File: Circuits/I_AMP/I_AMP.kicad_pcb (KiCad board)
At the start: 2 copper layers, 98 x 61 mm, 44 parts, among them P1 INPUT, P2 POWER, P5 GAIN ON/OFF, P6 OUTPUT (0-5V), U1 TL062, U2 LM393, U3 OPA277

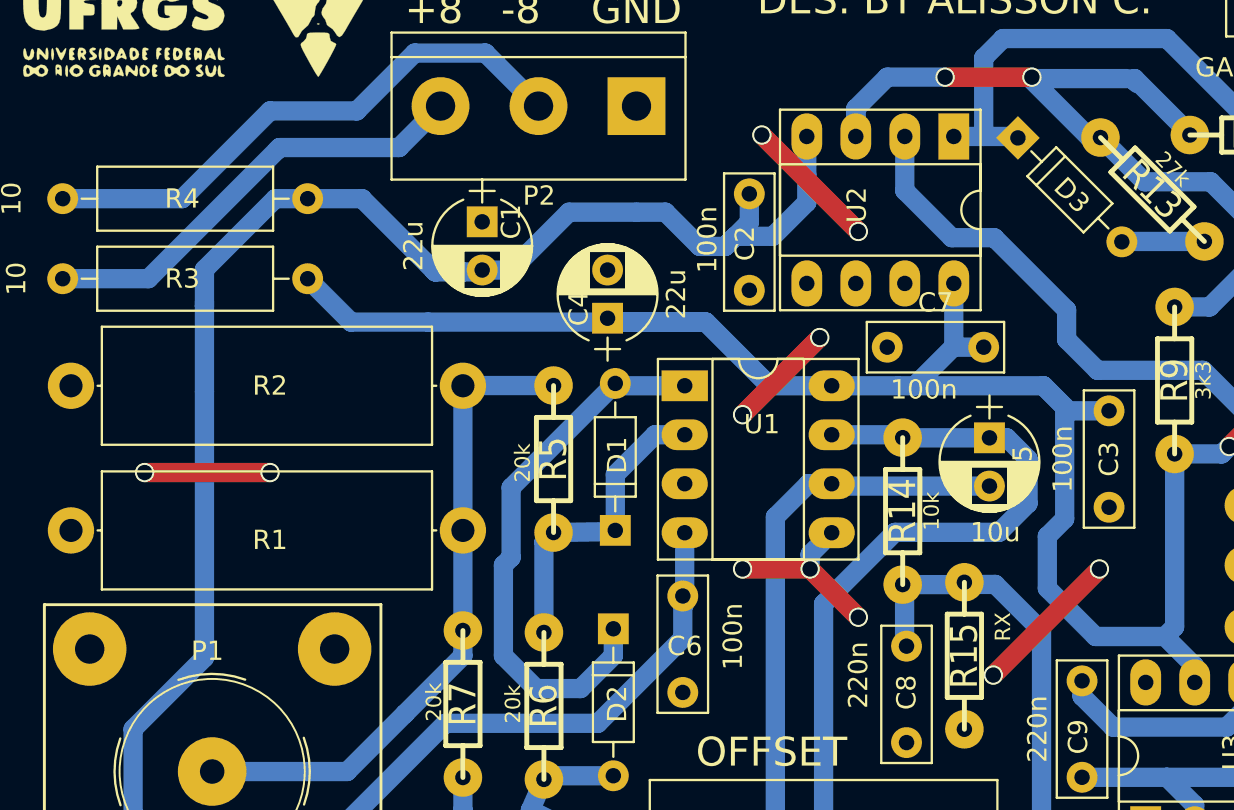
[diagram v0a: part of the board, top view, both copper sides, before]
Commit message: EDIT: Correction of some jumpers
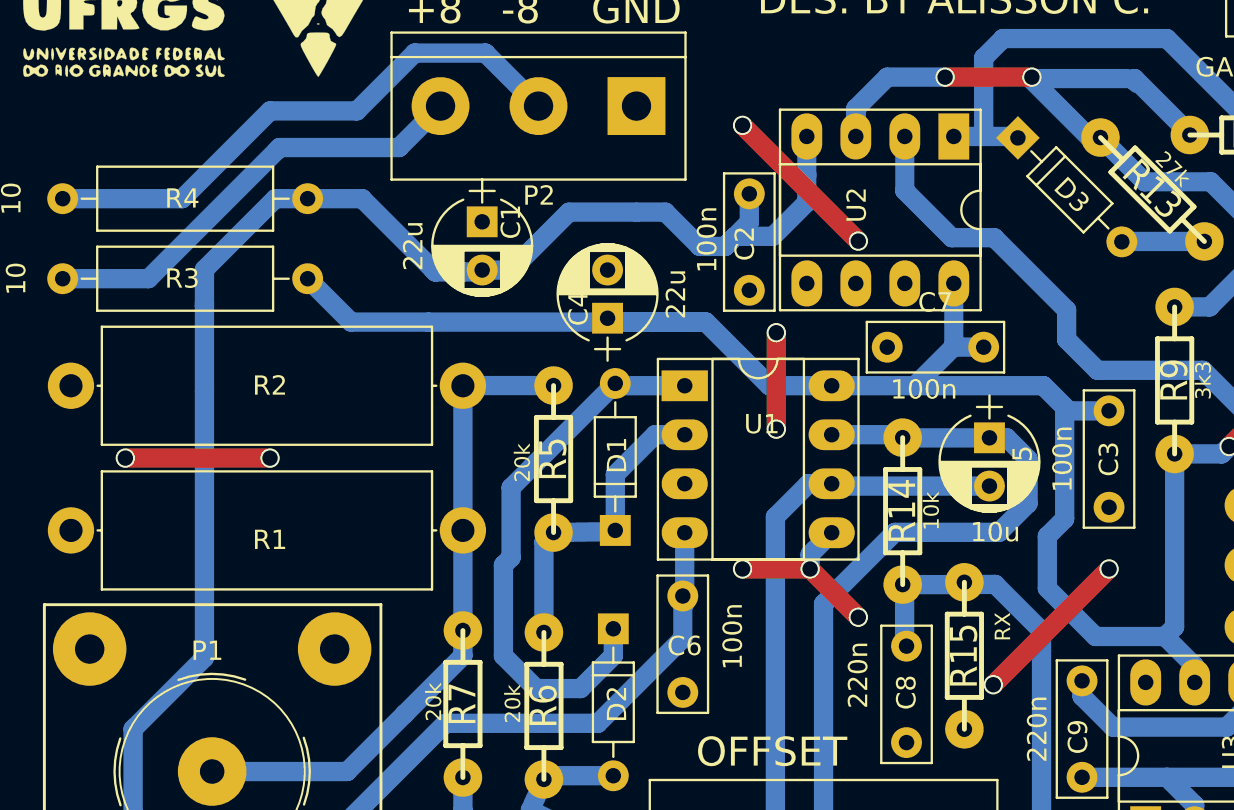
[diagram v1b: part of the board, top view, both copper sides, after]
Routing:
- net GND: track 36.4 -> 38.9 mm
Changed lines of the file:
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@@
   )
   (gr_line (start 67 102) (end 67 43.5) (angle 90) (layer Edge.Cuts) (width 0.15))
-  (via (at 110.5 67.5) (size 1) (drill 0.8) (layers F.Cu B.Cu) (net 1))
-  (via (at 106.5 71.5) (size 1) (drill 0.8) (layers F.Cu B.Cu) (net 1))
-  (segment (start 110.5 67.5) (end 106.5 71.5) (width 1) (layer F.Cu) (net 1))
-  (via (at 119.5 85) (size 1) (drill 0.8) (layers F.Cu B.Cu) (net 1))
-  (via (at 125 79.5) (size 1) (drill 0.8) (layers F.Cu B.Cu) (net 1))
-  (segment (start 119.5 85) (end 125 79.5) (width 1) (layer F.Cu) (net 1))
-  (via (at 112.5 62) (size 1) (drill 0.8) (layers F.Cu B.Cu) (net 1))
-  (via (at 107.5 57) (size 1) (drill 0.8) (layers F.Cu B.Cu) (net 1))
-  (segment (start 112.5 62) (end 107.5 57) (width 1) (layer F.Cu) (net 1))
-  (via (at 82 74.5) (size 1) (drill 0.8) (layers F.Cu B.Cu) (net 1))
-  (via (at 75.5 74.5) (size 1) (drill 0.8) (layers F.Cu B.Cu) (net 1))
-  (segment (start 82 74.5) (end 75.5 74.5) (width 1) (layer F.Cu) (net 1))
+  (via (at 119.5 85.5) (size 1) (drill 0.8) (layers F.Cu B.Cu) (net 1))
+  (via (at 125.5 79.5) (size 1) (drill 0.8) (layers F.Cu B.Cu) (net 1))
+  (segment (start 119.5 85.5) (end 125.5 79.5) (width 1) (layer F.Cu) (net 1))
+  (via (at 108.25 72.25) (size 1) (drill 0.8) (layers F.Cu B.Cu) (net 1))
+  (via (at 108.25 67.25) (size 1) (drill 0.8) (layers F.Cu B.Cu) (net 1))
+  (segment (start 108.25 72.25) (end 108.25 67.25) (width 1) (layer F.Cu) (net 1))
+  (via (at 82 73.75) (size 1) (drill 0.8) (layers F.Cu B.Cu) (net 1))
+  (via (at 74.5 73.75) (size 1) (drill 0.8) (layers F.Cu B.Cu) (net 1))
+  (segment (start 82 73.75) (end 74.5 73.75) (width 1) (layer F.Cu) (net 1))
+  (via (at 106.5 56.5) (size 1) (drill 0.8) (layers F.Cu B.Cu) (net 1))
+  (via (at 112.5 62.5) (size 1) (drill 0.8) (layers F.Cu B.Cu) (net 1))
+  (segment (start 106.5 56.5) (end 112.5 62.5) (width 1) (layer F.Cu) (net 1))
   (segment (start 110 79.5) (end 112.5 82) (width 1) (layer F.Cu) (net 1))
   (via (at 112.5 82) (size 1) (drill 0.8) (layers F.Cu B.Cu) (net 1))
@@
   (segment (start 103.5 77.62) (end 104.08 77.62) (width 1) (layer B.Cu) (net 2))
   (segment (start 103.5 81.3) (end 103.5 77.62) (width 1) (layer B.Cu) (net 2) (status 10))
-  (segment (start 111.12 70) (end 107.9 70) (width 1) (layer B.Cu) (net 3) (status 400000))
+  (segment (start 111.12 70) (end 107.9 70) (width 1) (layer B.Cu) (net 3))
   (segment (start 107.9 70) (end 104.6 66.7) (width 1) (layer B.Cu) (net 3))
-  (segment (start 104.6 66.7) (end 99.7 66.7) (width 1) (layer B.Cu) (net 3) (status 800000))
-  (segment (start 99.7 66.7) (end 99.5 66.5) (width 1) (layer B.Cu) (net 3) (status C00000))
+  (segment (start 104.6 66.7) (end 99.7 66.7) (width 1) (layer B.Cu) (net 3))
+  (segment (start 99.7 66.7) (end 99.5 66.5) (width 1) (layer B.Cu) (net 3))
   (segment (start 119 68) (end 117.475 68) (width 1) (layer B.Cu) (net 3))
   (segment (start 117.475 68) (end 117.45 67.975) (width 1) (layer B.Cu) (net 3))
@@
   (segment (start 123.2 76.9) (end 123.2 71.1) (width 1) (layer B.Cu) (net 3))
   (segment (start 111.12 70) (end 114.5 70) (width 1) (layer B.Cu) (net 3))
-  (segment (start 110.7 97.2) (end 115.7 97.2) (width 1) (layer B.Cu) (net 4) (status C00000))
+  (segment (start 110.7 97.2) (end 115.7 97.2) (width 1) (layer B.Cu) (net 4))
   (segment (start 119.3 72.7) (end 120.2 72.7) (width 1) (layer B.Cu) (net 4))
   (segment (start 110.7 81.3) (end 110.7 97.2) (width 1) (layer B.Cu) (net 4))
@@
   (segment (start 114.8 72.69) (end 114.65 72.54) (width 1) (layer B.Cu) (net 4) (status 30))
   (segment (start 114.65 72.54) (end 111.12 72.54) (width 1) (layer B.Cu) (net 4) (status 10))
-  (segment (start 92.19 97) (end 92.19 98.19) (width 1) (layer B.Cu) (net 5) (status 400000))
+  (segment (start 92.19 97) (end 92.19 98.19) (width 1) (layer B.Cu) (net 5))
   (segment (start 92.19 98.19) (end 93.8 99.8) (width 1) (layer B.Cu) (net 5))
   (segment (start 92 92) (end 92 93.81) (width 1) (layer B.Cu) (net 5))

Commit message: ADD: Current Sensor Fabrication Files
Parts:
- P5: value GAIN ON/OFF -> 2nd GAIN ON/OFF
- RV1, RV2: footprint Potentiometers:Potentiometer_Alps_RK163_Single_Vertical -> Potentiometers:Potentiometer_Trimmer_Bourns_3296X
- moved RV2 7.40 mm to (146.6, 54.5), turned to 180 degrees
- moved RV1 6.62 mm to (112.2, 96.2), turned to 180 degrees
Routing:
- net GND: track 38.9 -> 0.00 mm, vias 11 -> 0
- net Net-(R10-Pad1): track 43.6 -> 35.7 mm
- net Net-(R16-Pad2): track 66.3 -> 59.0 mm
- net Net-(R12-Pad1): track 5.97 -> 12.8 mm
- net +8V: track 108.6 -> 102.6 mm, vias 2 -> 6
- net Net-(P5-Pad1): track 20.2 -> 15.3 mm
- net Net-(D2-Pad2): track 10.3 -> 7.87 mm
- net -8V: track 176.5 -> 174.9 mm, vias 0 -> 2
- net I_RECTF: track 46.7 -> 45.2 mm, vias 0 -> 2
- net Net-(C8-Pad1): track 35.8 -> 34.5 mm, vias 0 -> 2
- net Net-(C9-Pad2): track 29.8 -> 28.5 mm
- net Net-(P2-Pad2): track 28.9 -> 29.6 mm
- net Net-(C5-Pad2): track 60.1 -> 59.9 mm, vias 0 -> 4
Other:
- board size 98 x 61 mm -> 98 x 61.5 mm
- board text added: "2nd GAIN ADJ. (1-10x)"
- board text added: "Designed by Alisson Claudino"
- board text added: "SADAMAP CURRENT SENSOR"
- board text removed: "DES. BY ALISSON C."
- board text removed: "GAIN ADJ."
- board text removed: "SADAMAP CURRENT AMP."

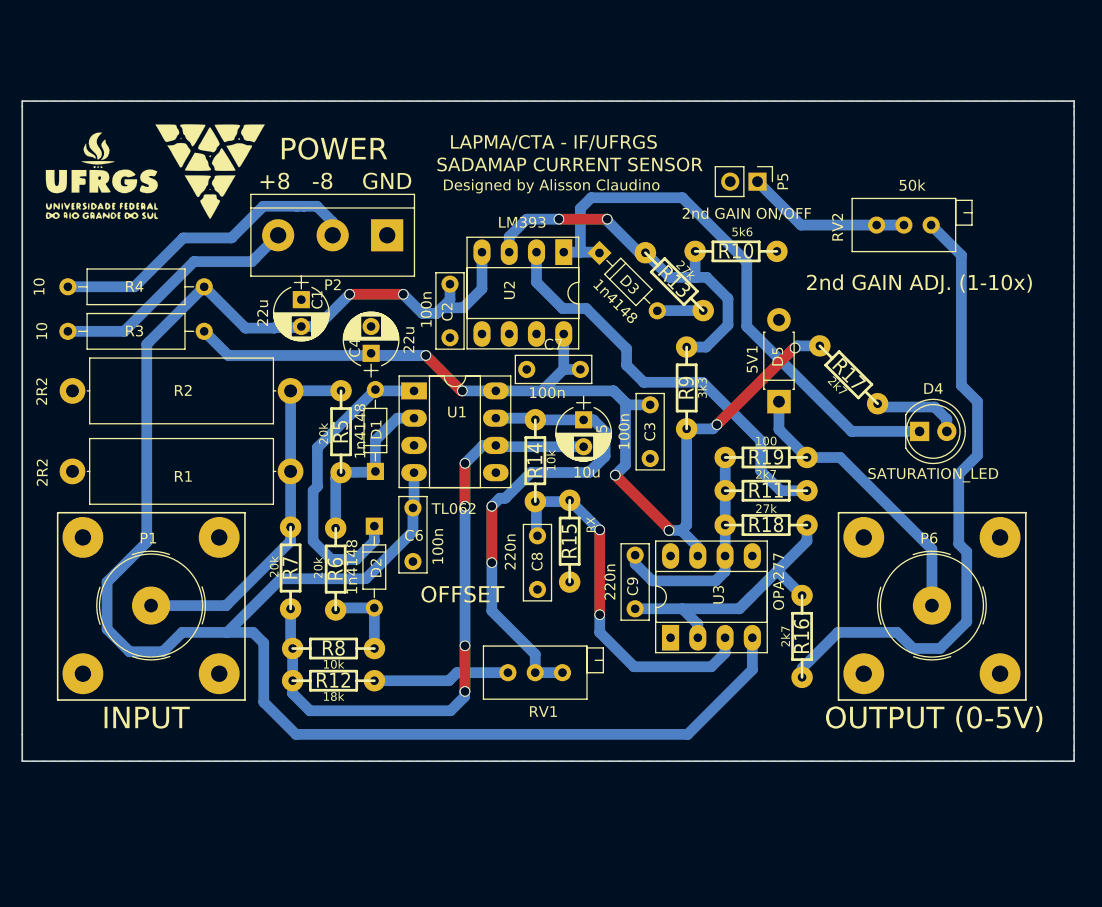
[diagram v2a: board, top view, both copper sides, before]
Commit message: EDIT: Correction of the Current Sensor board
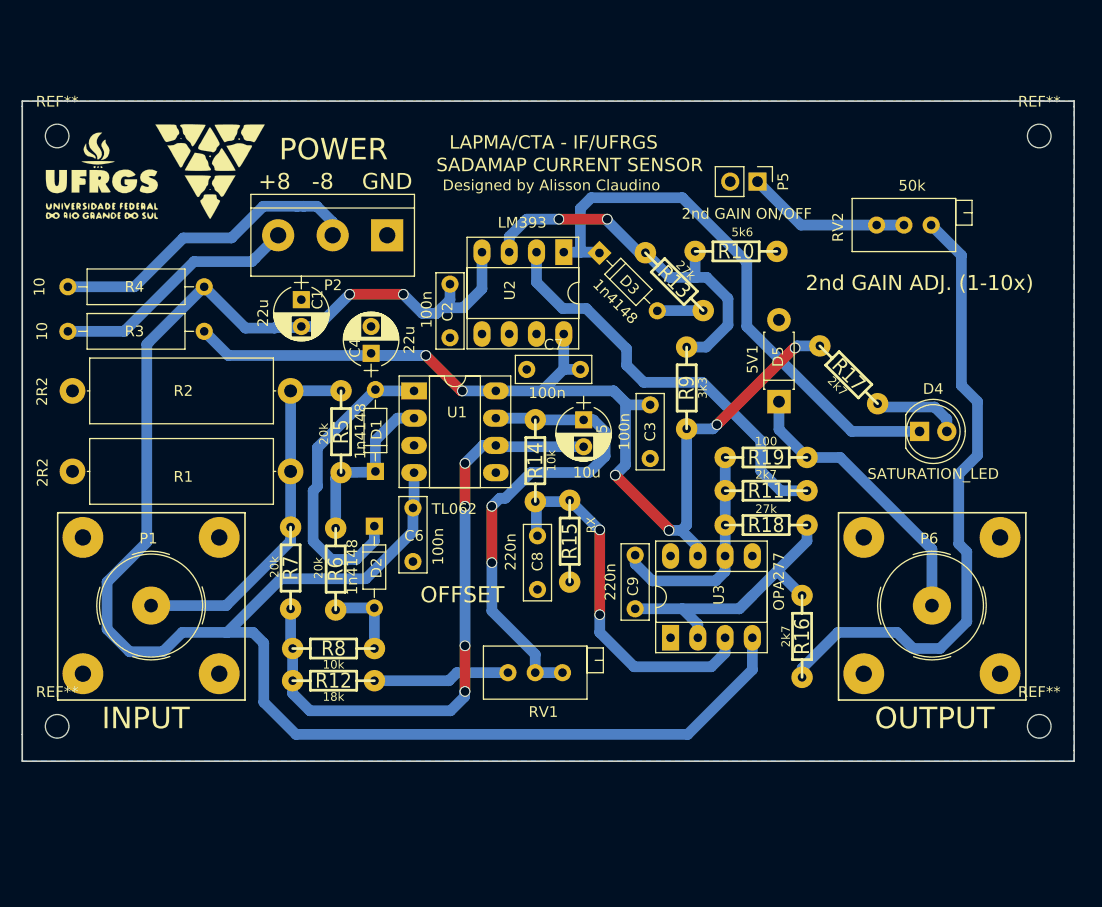
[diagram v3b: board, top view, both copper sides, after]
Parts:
- added REF**: MountingHole_2.2mm_M2, Mounting_Holes:MountingHole_2.2mm_M2, F.Cu at (161.8, 101.2)
- added REF**: MountingHole_2.2mm_M2, Mounting_Holes:MountingHole_2.2mm_M2, F.Cu at (70.2, 101.2)
- added REF**: MountingHole_2.2mm_M2, Mounting_Holes:MountingHole_2.2mm_M2, F.Cu at (70.2, 46.2)
- added REF**: MountingHole_2.2mm_M2, Mounting_Holes:MountingHole_2.2mm_M2, F.Cu at (161.8, 46.2)
- P6: value OUTPUT (0-5V) -> OUTPUT
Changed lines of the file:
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@@
     (links 84)
     (no_connects 0)
-    (area 66.924999 42.924999 165.075001 104.575001)
+    (area 60.292857 41.675 174.85 120.700001)
     (thickness 1.6)
     (drawings 18)
     (tracks 272)
     (zones 0)
-    (modules 44)
+    (modules 48)
     (nets 24)
   )
@@
     (visible_elements FFFFFF7F)
     (pcbplotparams
-      (layerselection 0x00030_80000001)
+      (layerselection 0x00000_00000000)
       (usegerberextensions false)
       (excludeedgelayer true)
@@
       (viasonmask false)
       (mode 1)
-      (useauxorigin false)
+      (useauxorigin true)
       (hpglpennumber 1)
       (hpglpenspeed 20)
@@
       (outputformat 1)
       (mirror false)
-      (drillshape 1)
+      (drillshape 0)
       (scaleselection 1)
-      (outputdirectory ""))
+      (outputdirectory "/home/alissomc/SADAMAP/Circuits/I_AMP/Fabrication Files/Gerbers/"))
   )
   (net 0 "")
@@
     (add_net "Net-(R16-Pad2)")
     (add_net V1_I)
+  )
+  (module Mounting_Holes:MountingHole_2.2mm_M2 (layer F.Cu)
+    (at 161.75 101.25)
+    (descr "Mounting Hole 2.2mm, no annular, M2")
+    (tags "mounting hole 2.2mm no annular m2")
+    (fp_text reference REF** (at 0 -3.2) (layer F.SilkS)
+      (effects (font (size 1 1) (thickness 0.15)))
+    )
+    (fp_text value MountingHole_2.2mm_M2 (at 0 3.2) (layer F.Fab) hide
+      (effects (font (size 1 1) (thickness 0.15)))
+    )
+    (fp_circle (center 0 0) (end 2.2 0) (layer Cmts.User) (width 0.15))
+    (fp_circle (center 0 0) (end 2.45 0) (layer F.CrtYd) (width 0.05))
+    (pad 1 np_thru_hole circle (at 0 0) (size 2.2 2.2) (drill 2.2) (layers *.Cu *.Mask))
+  )
+  (module Mounting_Holes:MountingHole_2.2mm_M2 (layer F.Cu)
+    (at 70.25 101.25)
+    (descr "Mounting Hole 2.2mm, no annular, M2")
+    (tags "mounting hole 2.2mm no annular m2")
+    (fp_text reference REF** (at 0 -3.2) (layer F.SilkS)
+      (effects (font (size 1 1) (thickness 0.15)))
+    )
+    (fp_text value MountingHole_2.2mm_M2 (at 0 3.2) (layer F.Fab) hide
+      (effects (font (size 1 1) (thickness 0.15)))
+    )
+    (fp_circle (center 0 0) (end 2.2 0) (layer Cmts.User) (width 0.15))
+    (fp_circle (center 0 0) (end 2.45 0) (layer F.CrtYd) (width 0.05))
+    (pad 1 np_thru_hole circle (at 0 0) (size 2.2 2.2) (drill 2.2) (layers *.Cu *.Mask))
+  )
+  (module Mounting_Holes:MountingHole_2.2mm_M2 (layer F.Cu)
+    (at 70.25 46.25)
+    (descr "Mounting Hole 2.2mm, no annular, M2")
+    (tags "mounting hole 2.2mm no annular m2")
+    (fp_text reference REF** (at 0 -3.2) (layer F.SilkS)
+      (effects (font (size 1 1) (thickness 0.15)))
+    )
+    (fp_text value MountingHole_2.2mm_M2 (at 0 3.2) (layer F.Fab) hide
+      (effects (font (size 1 1) (thickness 0.15)))
+    )
+    (fp_circle (center 0 0) (end 2.2 0) (layer Cmts.User) (width 0.15))
+    (fp_circle (center 0 0) (end 2.45 0) (layer F.CrtYd) (width 0.05))
+    (pad 1 np_thru_hole circle (at 0 0) (size 2.2 2.2) (drill 2.2) (layers *.Cu *.Mask))
   )
   (module Resistors_THT:R_Axial_DIN0309_L9.0mm_D3.2mm_P12.70mm_Horizontal (layer F.Cu)
@@
       (effects (font (size 1 1) (thickness 0.15)))
     )
-    (fp_text value "OUTPUT (0-5V)" (at 0.25 10.5) (layer F.SilkS)
+    (fp_text value "OUTPUT " (at 0.25 10.5) (layer F.SilkS)
       (effects (font (size 2 2) (thickness 0.3)))
     )
@@
     )
   )
+  (module Mounting_Holes:MountingHole_2.2mm_M2 (layer F.Cu)
+    (at 161.75 46.25)
+    (descr "Mounting Hole 2.2mm, no annular, M2")
+    (tags "mounting hole 2.2mm no annular m2")
+    (fp_text reference REF** (at 0 -3.2) (layer F.SilkS)
+      (effects (font (size 1 1) (thickness 0.15)))
+    )
+    (fp_text value MountingHole_2.2mm_M2 (at 0 3.2) (layer F.Fab) hide
+      (effects (font (size 1 1) (thickness 0.15)))
+    )
+    (fp_circle (center 0 0) (end 2.2 0) (layer Cmts.User) (width 0.15))
+    (fp_circle (center 0 0) (end 2.45 0) (layer F.CrtYd) (width 0.05))
+    (pad 1 np_thru_hole circle (at 0 0) (size 2.2 2.2) (drill 2.2) (layers *.Cu *.Mask))
+  )
   (gr_line (start 67 43.5) (end 67 43) (angle 90) (layer Edge.Cuts) (width 0.15))
   (gr_line (start 165 43.5) (end 165 43) (angle 90) (layer Edge.Cuts) (width 0.15))
@@
   (segment (start 74.9 92.2) (end 74.9 87.8) (width 1) (layer B.Cu) (net 2))
   (segment (start 74.9 87.8) (end 78.6 84.1) (width 1) (layer B.Cu) (net 2))
-  (segment (start 83.95 60.3) (end 78.75 65.5) (width 1) (layer B.Cu) (net 2) (status 400000))
-  (segment (start 83.95 60.3) (end 87.8 64.15) (width 1) (layer B.Cu) (net 2) (status 400000))
+  (segment (start 83.95 60.3) (end 78.75 65.5) (width 1) (layer B.Cu) (net 2))
+  (segment (start 83.95 60.3) (end 87.8 64.15) (width 1) (layer B.Cu) (net 2))
   (segment (start 90.575 64.1) (end 92.9 64.1) (width 1) (layer B.Cu) (net 2) (status 20))
   (segment (start 90.525 64.15) (end 90.575 64.1) (width 1) (layer B.Cu) (net 2))
@@
   (segment (start 132.49 82.5) (end 132.49 85.37) (width 1) (layer B.Cu) (net 7) (status 30))
   (segment (start 132.49 85.37) (end 132.48 85.38) (width 1) (layer B.Cu) (net 7) (status 30))
-  (segment (start 139.65 89.065) (end 137.3425 86.7575) (width 1) (layer B.Cu) (net 8) (status 400000))
+  (segment (start 139.65 89.065) (end 137.3425 86.7575) (width 1) (layer B.Cu) (net 8))
   (segment (start 137.4 86.75) (end 137.4 86.7) (width 1) (layer B.Cu) (net 8))
   (segment (start 137.3925 86.7575) (end 137.4 86.75) (width 1) (layer B.Cu) (net 8))
@@
   (segment (start 99.9 69.88) (end 100.02 70) (width 1) (layer B.Cu) (net 10) (status 30))
   (segment (start 100.02 70) (end 103.5 70) (width 1) (layer B.Cu) (net 10) (status 30))
-  (segment (start 99.81 94) (end 99.81 90.23) (width 1) (layer B.Cu) (net 11) (status C00000))
-  (segment (start 99.81 90.23) (end 99.8 90.22) (width 1) (layer B.Cu) (net 11) (status C00000))
+  (segment (start 99.81 94) (end 99.81 90.23) (width 1) (layer B.Cu) (net 11))
+  (segment (start 99.81 90.23) (end 99.8 90.22) (width 1) (layer B.Cu) (net 11))
   (segment (start 99.9 90.22) (end 96.39 90.22) (width 1) (layer B.Cu) (net 11) (status 30))
   (segment (start 96.39 90.22) (end 96.2 90.41) (width 1) (layer B.Cu) (net 11) (status 30))
@@
   (segment (start 152 71.5) (end 153.14 72.64) (width 1) (layer B.Cu) (net 14))
   (segment (start 153.14 72.64) (end 153.14 73.775) (width 1) (layer B.Cu) (net 14) (status 20))
-  (segment (start 137.5 71) (end 137.5 73.59) (width 1) (layer B.Cu) (net 15) (status 400000))
-  (segment (start 137.5 73.59) (end 140.11 76.2) (width 1) (layer B.Cu) (net 15) (status 800000))
+  (segment (start 137.5 71) (end 137.5 73.59) (width 1) (layer B.Cu) (net 15))
+  (segment (start 137.5 73.59) (end 140.11 76.2) (width 1) (layer B.Cu) (net 15))
   (segment (start 137.5 71.4) (end 137.5 71) (width 1) (layer B.Cu) (net 15) (status 30))
   (segment (start 140.11 76.2) (end 143.2 76.2) (width 1) (layer B.Cu) (net 15) (status 10))
@@
   (segment (start 89.45 52.8) (end 92.6 52.8) (width 1) (layer B.Cu) (net 17))
   (segment (start 92.6 52.8) (end 93.22 52.8) (width 1) (layer B.Cu) (net 17))
-  (segment (start 94.45 52.8) (end 95.92 54.27) (width 1) (layer B.Cu) (net 17) (status 800000))
-  (segment (start 95.92 54.27) (end 95.92 55.5) (width 1) (layer B.Cu) (net 17) (status C00000))
+  (segment (start 94.45 52.8) (end 95.92 54.27) (width 1) (layer B.Cu) (net 17))
+  (segment (start 95.92 54.27) (end 95.92 55.5) (width 1) (layer B.Cu) (net 17))
   (segment (start 83 57.95) (end 88.39 57.95) (width 1) (layer B.Cu) (net 18))
   (segment (start 76.6 64.35) (end 83 57.95) (width 1) (layer B.Cu) (net 18))
   (segment (start 90.84 55.5) (end 88.69 57.65) (width 1) (layer B.Cu) (net 18) (status 20))
   (segment (start 76.5 64.45) (end 76.6 64.35) (width 1) (layer B.Cu) (net 18))
-  (segment (start 76.5 64.45) (end 71.25 64.45) (width 1) (layer B.Cu) (net 18) (status 800000))
+  (segment (start 76.5 64.45) (end 71.25 64.45) (width 1) (layer B.Cu) (net 18))
   (segment (start 88.39 57.95) (end 88.69 57.65) (width 1) (layer B.Cu) (net 18))
   (segment (start 149.14 54.55) (end 146.6 54.55) (width 1) (layer B.Cu) (net 19) (status 30))
